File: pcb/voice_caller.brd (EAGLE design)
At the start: 56.5 x 59.1 mm, 36 parts, among them IC1 PRO_MICRO, IC2 AT45DB321D-S, IC3 78L12SMD, K1 TQ2SA-L2-5V

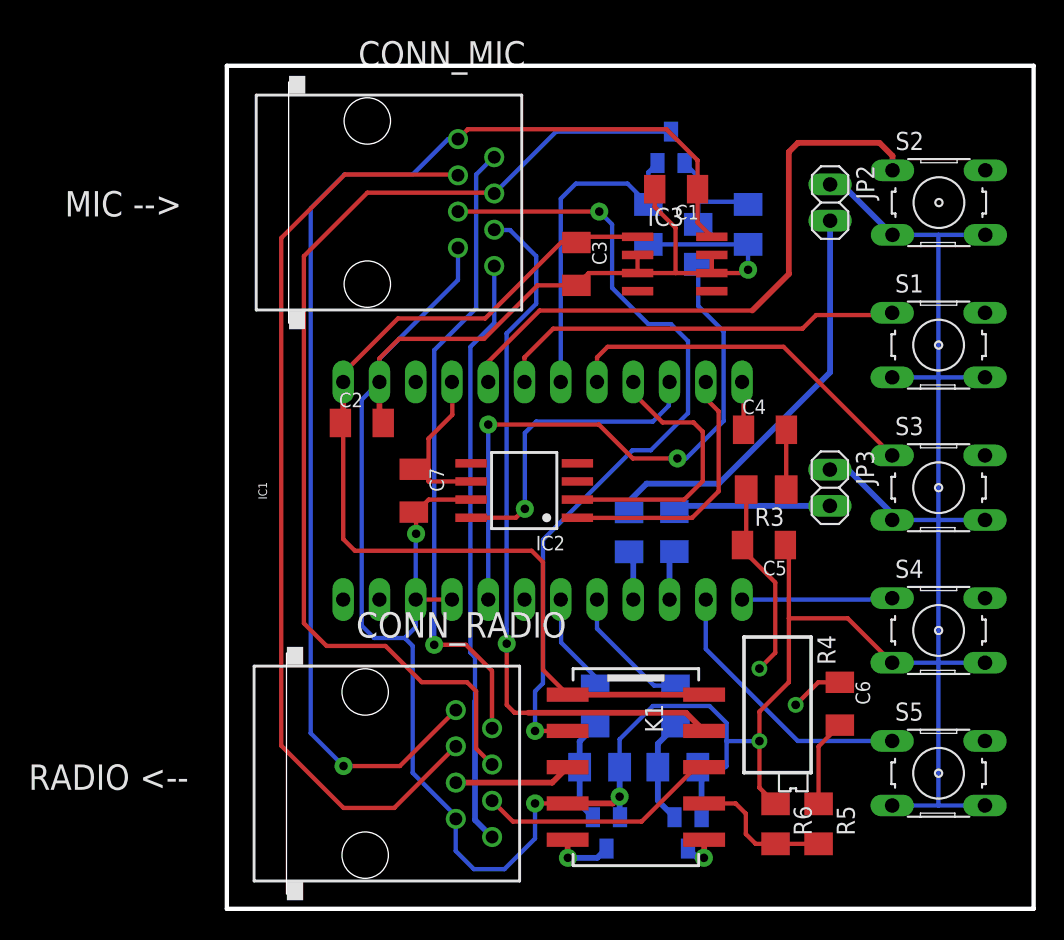
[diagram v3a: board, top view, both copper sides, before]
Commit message: Mounting holes
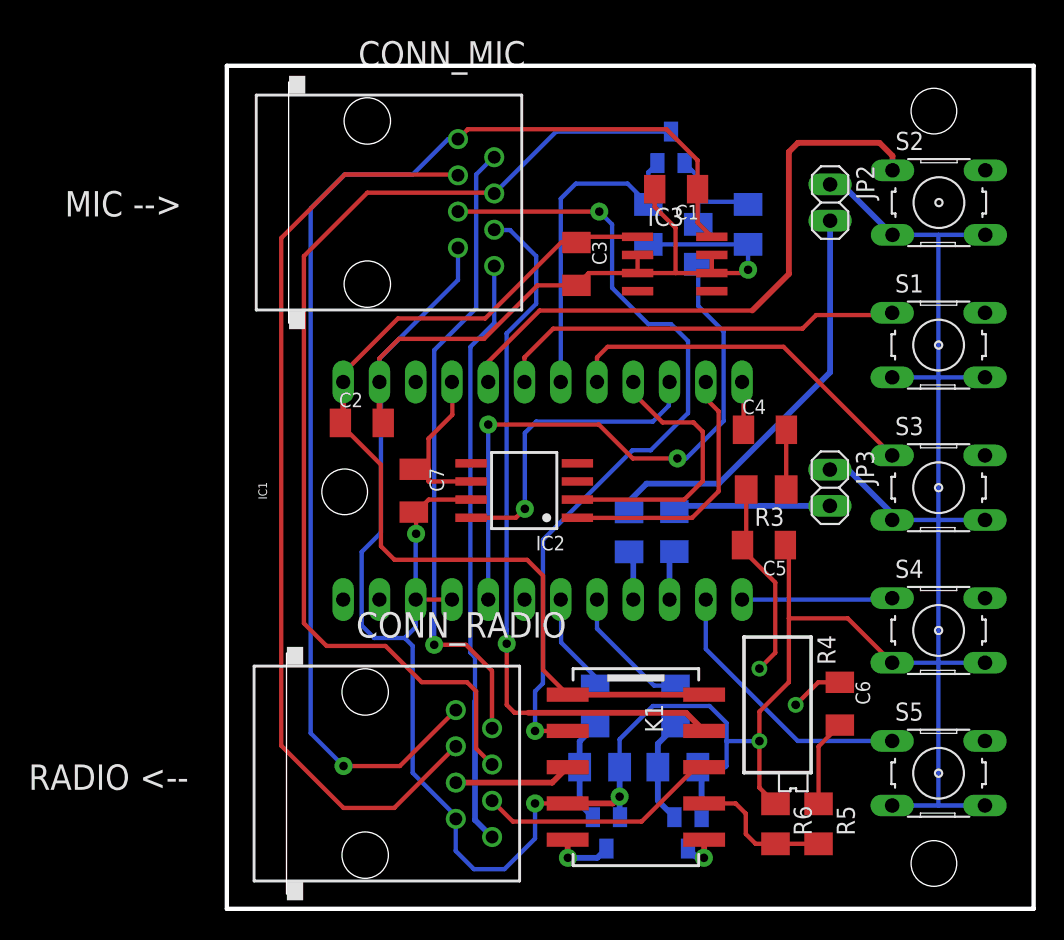
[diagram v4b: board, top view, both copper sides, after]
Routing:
- net +5V: track 70.8 -> 69.1 mm
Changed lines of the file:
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@@
 <layer number="42" name="bRestrict" color="1" fill="10" visible="yes" active="yes"/>
 <layer number="43" name="vRestrict" color="2" fill="10" visible="yes" active="yes"/>
-<layer number="44" name="Drills" color="7" fill="1" visible="no" active="yes"/>
-<layer number="45" name="Holes" color="7" fill="1" visible="no" active="yes"/>
+<layer number="44" name="Drills" color="7" fill="1" visible="yes" active="yes"/>
+<layer number="45" name="Holes" color="7" fill="1" visible="yes" active="yes"/>
 <layer number="46" name="Milling" color="3" fill="1" visible="no" active="yes"/>
 <layer number="47" name="Measures" color="7" fill="1" visible="no" active="yes"/>
@@
 <wire x1="62.865" y1="5.715" x2="62.865" y2="64.77" width="0.3048" layer="20"/>
 <wire x1="62.865" y1="64.77" x2="6.35" y2="64.77" width="0.3048" layer="20"/>
+<hole x="55.88" y="8.89" drill="3.2"/>
+<hole x="55.88" y="61.595" drill="3.2"/>
+<hole x="14.605" y="34.925" drill="3.2"/>
 </plain>
 <attributes>
@@
 <contactref element="K1" pad="10"/>
 <wire x1="39.784375" y1="20.716875" x2="30.224375" y2="20.716875" width="0.4064" layer="1"/>
-<wire x1="14.5" y1="39.752528125" x2="14.5" y2="31.616875" width="0.3048" layer="1"/>
-<wire x1="14.5" y1="31.616875" x2="15.319375" y2="30.7975" width="0.3048" layer="1"/>
-<wire x1="15.319375" y1="30.7975" x2="27.701875" y2="30.7975" width="0.3048" layer="1"/>
-<wire x1="27.701875" y1="30.7975" x2="28.495625" y2="30.00375" width="0.3048" layer="1"/>
-<wire x1="28.495625" y1="30.00375" x2="28.495625" y2="22.445625" width="0.3048" layer="1"/>
+<wire x1="27.384375" y1="30.1625" x2="28.495625" y2="29.05125" width="0.3048" layer="1"/>
+<wire x1="28.495625" y1="29.05125" x2="28.495625" y2="22.445625" width="0.3048" layer="1"/>
 <wire x1="28.495625" y1="22.445625" x2="30.224375" y2="20.716875" width="0.3048" layer="1"/>
 <wire x1="29.766875" y1="52.38875" x2="30.8375" y2="52.38875" width="0.3048" layer="1"/>
+<wire x1="27.384375" y1="30.1625" x2="18.0975" y2="30.1625" width="0.3048" layer="1"/>
+<wire x1="18.0975" y1="30.1625" x2="17.145" y2="31.115" width="0.3048" layer="1"/>
+<wire x1="17.145" y1="31.115" x2="17.145" y2="36.83" width="0.3048" layer="1"/>
+<wire x1="17.145" y1="36.83" x2="14.303696875" y2="39.671303125" width="0.3048" layer="1"/>
+<wire x1="14.303696875" y1="39.671303125" x2="14.303696875" y2="39.752528125" width="0.3048" layer="1"/>
 </signal>
 <signal name="GND">
@@
 <wire x1="18.811875" y1="24.685625" x2="16.66875" y2="24.685625" width="0.3048" layer="16"/>
 <wire x1="16.66875" y1="24.685625" x2="15.795625" y2="25.55875" width="0.3048" layer="16"/>
-<wire x1="15.795625" y1="25.55875" x2="15.795625" y2="41.375625" width="0.3048" layer="16"/>
-<wire x1="15.795625" y1="41.375625" x2="17.04" y2="42.62" width="0.3048" layer="16"/>
 <wire x1="17.04" y1="42.62" x2="17.04" y2="44.265625" width="0.3048" layer="16"/>
 <wire x1="17.04" y1="44.265625" x2="22.5425" y2="49.768125" width="0.3048" layer="16"/>
@@
 <wire x1="48.6085875" y1="56.458184375" x2="49.448140625" y2="56.458184375" width="0.4064" layer="16"/>
 <wire x1="49.448140625" y1="56.458184375" x2="52.9813" y2="52.925025" width="0.4064" layer="16"/>
+<wire x1="17.04" y1="42.62" x2="17.145" y2="42.515" width="0.3048" layer="16"/>
+<wire x1="17.145" y1="42.515" x2="17.145" y2="32.0675" width="0.3048" layer="16"/>
+<wire x1="17.145" y1="32.0675" x2="15.795625" y2="30.718125" width="0.3048" layer="16"/>
+<wire x1="15.795625" y1="30.718125" x2="15.795625" y2="25.55875" width="0.3048" layer="16"/>
 </signal>
 <signal name="MOSI">

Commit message: Missing nets for flash routed.
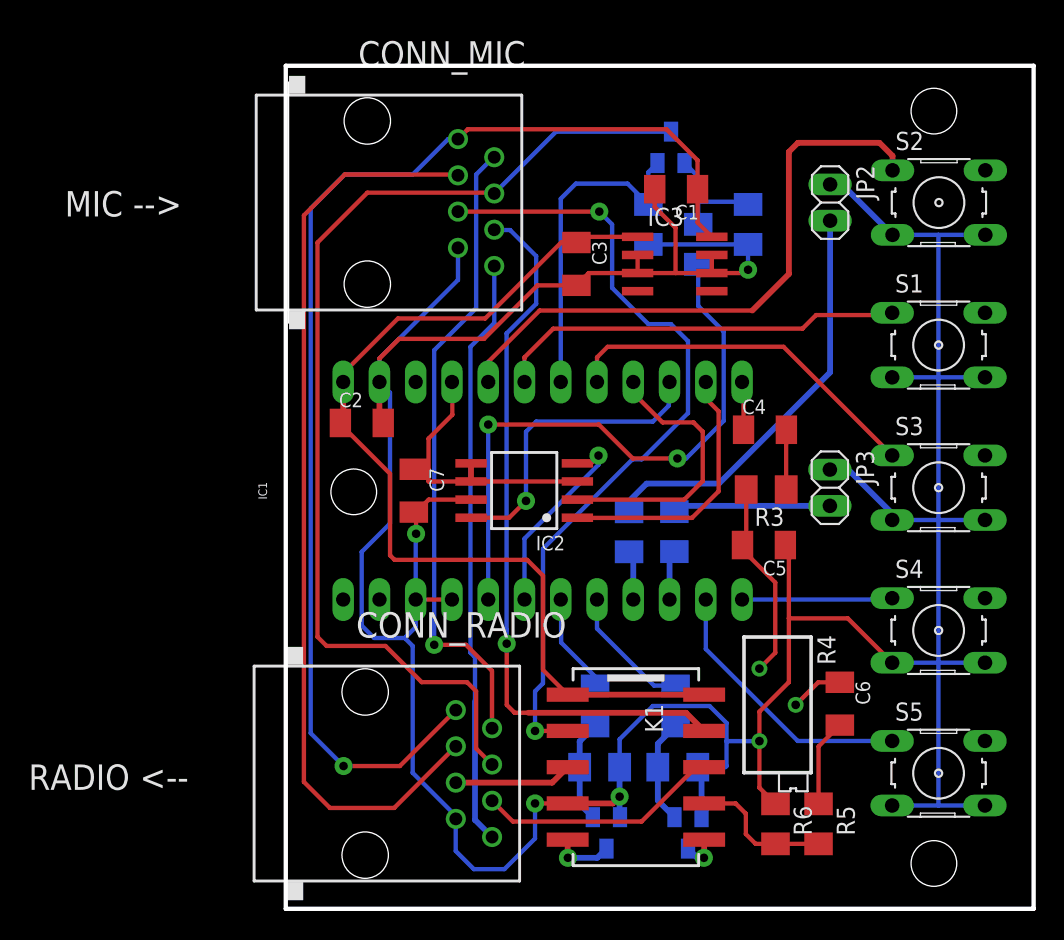
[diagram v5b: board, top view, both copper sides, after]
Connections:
- removed net N$7: IC2.5
- removed net N$8: IC2.3
- net +3V3: now also IC2.3, IC2.5
- net FLASH_CS: now also IC1.6
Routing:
- net FLASH_CS: track 0.00 -> 14.2 mm, vias 0 -> 1
- net +3V3: track 11.7 -> 20.4 mm
- net PTT: track 74.7 -> 73.9 mm
- net AF_OUT: track 65.6 -> 64.9 mm
- net GND: track 270.6 -> 271.2 mm
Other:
- board size 56.5 x 59.1 mm -> 52.4 x 59.1 mm
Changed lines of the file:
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@@
 <layer number="42" name="bRestrict" color="1" fill="10" visible="yes" active="yes"/>
 <layer number="43" name="vRestrict" color="2" fill="10" visible="yes" active="yes"/>
-<layer number="44" name="Drills" color="7" fill="1" visible="yes" active="yes"/>
-<layer number="45" name="Holes" color="7" fill="1" visible="yes" active="yes"/>
+<layer number="44" name="Drills" color="7" fill="1" visible="no" active="yes"/>
+<layer number="45" name="Holes" color="7" fill="1" visible="no" active="yes"/>
 <layer number="46" name="Milling" color="3" fill="1" visible="no" active="yes"/>
 <layer number="47" name="Measures" color="7" fill="1" visible="no" active="yes"/>
@@
 <text x="-5.000625" y="54.213125" size="1.778" layer="21">MIC --&gt;</text>
 <text x="-7.540625" y="14.049375" size="1.778" layer="21">RADIO &lt;--</text>
-<wire x1="6.35" y1="64.77" x2="6.35" y2="5.715" width="0.3048" layer="20"/>
-<wire x1="6.35" y1="5.715" x2="62.865" y2="5.715" width="0.3048" layer="20"/>
+<wire x1="10.4775" y1="64.77" x2="10.4775" y2="5.715" width="0.3048" layer="20"/>
+<wire x1="10.4775" y1="5.715" x2="62.865" y2="5.715" width="0.3048" layer="20"/>
 <wire x1="62.865" y1="5.715" x2="62.865" y2="64.77" width="0.3048" layer="20"/>
-<wire x1="62.865" y1="64.77" x2="6.35" y2="64.77" width="0.3048" layer="20"/>
+<wire x1="62.865" y1="64.77" x2="10.4775" y2="64.77" width="0.3048" layer="20"/>
 <hole x="55.88" y="8.89" drill="3.2"/>
 <hole x="55.88" y="61.595" drill="3.2"/>
-<hole x="14.605" y="34.925" drill="3.2"/>
+<hole x="15.24" y="34.925" drill="3.2"/>
 </plain>
 <attributes>
@@
 </class>
 </classes>
-<designrules name="default">
+<designrules name="default *">
 <description language="de">&lt;b&gt;EAGLE Design Rules&lt;/b&gt;
 &lt;p&gt;
@@
 <param name="mdPadVia" value="8mil"/>
 <param name="mdViaVia" value="8mil"/>
-<param name="mdSmdPad" value="8mil"/>
-<param name="mdSmdVia" value="8mil"/>
-<param name="mdSmdSmd" value="8mil"/>
+<param name="mdSmdPad" value="0mil"/>
+<param name="mdSmdVia" value="0mil"/>
+<param name="mdSmdSmd" value="0mil"/>
 <param name="mdViaViaSameLayer" value="8mil"/>
 <param name="mnLayersViaInSmd" value="2"/>
@@
 <wire x1="29.766875" y1="52.38875" x2="30.8375" y2="52.38875" width="0.3048" layer="1"/>
 <wire x1="27.384375" y1="30.1625" x2="18.0975" y2="30.1625" width="0.3048" layer="1"/>
-<wire x1="18.0975" y1="30.1625" x2="17.145" y2="31.115" width="0.3048" layer="1"/>
-<wire x1="17.145" y1="31.115" x2="17.145" y2="36.83" width="0.3048" layer="1"/>
-<wire x1="17.145" y1="36.83" x2="14.303696875" y2="39.671303125" width="0.3048" layer="1"/>
+<wire x1="18.0975" y1="30.1625" x2="17.78" y2="30.48" width="0.3048" layer="1"/>
+<wire x1="17.78" y1="30.48" x2="17.78" y2="36.195" width="0.3048" layer="1"/>
+<wire x1="17.78" y1="36.195" x2="14.303696875" y2="39.671303125" width="0.3048" layer="1"/>
 <wire x1="14.303696875" y1="39.671303125" x2="14.303696875" y2="39.752528125" width="0.3048" layer="1"/>
 </signal>
@@
 <wire x1="48.6085875" y1="56.458184375" x2="49.448140625" y2="56.458184375" width="0.4064" layer="16"/>
 <wire x1="49.448140625" y1="56.458184375" x2="52.9813" y2="52.925025" width="0.4064" layer="16"/>
-<wire x1="17.04" y1="42.62" x2="17.145" y2="42.515" width="0.3048" layer="16"/>
-<wire x1="17.145" y1="42.515" x2="17.145" y2="32.0675" width="0.3048" layer="16"/>
-<wire x1="17.145" y1="32.0675" x2="15.795625" y2="30.718125" width="0.3048" layer="16"/>
+<wire x1="17.04" y1="42.62" x2="17.78" y2="41.88" width="0.3048" layer="16"/>
+<wire x1="17.78" y1="41.88" x2="17.78" y2="32.7025" width="0.3048" layer="16"/>
+<wire x1="17.78" y1="32.7025" x2="15.795625" y2="30.718125" width="0.3048" layer="16"/>
 <wire x1="15.795625" y1="30.718125" x2="15.795625" y2="25.55875" width="0.3048" layer="16"/>
 </signal>
@@
 <contactref element="IC2" pad="8"/>
 <contactref element="IC1" pad="15"/>
-<wire x1="23.455" y1="33.11" x2="26.60125" y2="33.11" width="0.3048" layer="1"/>
-<wire x1="26.60125" y1="33.11" x2="27.225625" y2="33.734375" width="0.3048" layer="1"/>
-<wire x1="27.225625" y1="33.734375" x2="27.225625" y2="39.0525" width="0.3048" layer="16"/>
-<wire x1="27.225625" y1="39.0525" x2="28.019375" y2="39.84625" width="0.3048" layer="16"/>
 <wire x1="28.019375" y1="39.84625" x2="36.195" y2="39.84625" width="0.3048" layer="16"/>
 <wire x1="36.195" y1="39.84625" x2="37.30625" y2="40.9575" width="0.3048" layer="16"/>
 <wire x1="37.30625" y1="40.9575" x2="37.30625" y2="42.56625" width="0.3048" layer="16"/>
 <wire x1="37.30625" y1="42.56625" x2="37.36" y2="42.62" width="0.3048" layer="16"/>
-<via x="27.225625" y="33.734375" extent="1-16" drill="0.6" diameter="1.27" shape="square"/>
+<wire x1="23.455" y1="33.11" x2="26.125" y2="33.11" width="0.3048" layer="1"/>
+<wire x1="26.125" y1="33.11" x2="27.305" y2="34.29" width="0.3048" layer="1"/>
+<via x="27.305" y="34.29" extent="1-16" drill="0.6" diameter="1.27" shape="square"/>
+<wire x1="27.305" y1="34.29" x2="27.305" y2="39.131875" width="0.3048" layer="16"/>
+<wire x1="27.305" y1="39.131875" x2="28.019375" y2="39.84625" width="0.3048" layer="16"/>
 </signal>
 <signal name="SCK">
@@
 <signal name="FLASH_CS">
 <contactref element="IC2" pad="4"/>
-</signal>
-<signal name="N$7">
-<contactref element="IC2" pad="5"/>
-</signal>
-<signal name="N$8">
-<contactref element="IC2" pad="3"/>
+<contactref element="IC1" pad="6"/>
+<via x="32.385" y="37.465" extent="1-16" drill="0.6" diameter="1.27" shape="square"/>
+<wire x1="27.2" y1="27.38" x2="27.2" y2="31.645" width="0.3048" layer="16"/>
+<wire x1="27.2" y1="31.645" x2="32.385" y2="36.83" width="0.3048" layer="16"/>
+<wire x1="32.385" y1="36.83" x2="32.385" y2="37.465" width="0.3048" layer="16"/>
+<wire x1="30.905" y1="36.92" x2="30.7975" y2="37.0275" width="0.3048" layer="1"/>
+<wire x1="30.7975" y1="37.0275" x2="31.9475" y2="37.0275" width="0.3048" layer="1"/>
+<wire x1="31.9475" y1="37.0275" x2="32.385" y2="37.465" width="0.3048" layer="1"/>
 </signal>
 <signal name="PTT">
@@
 <wire x1="25.08" y1="55.825" x2="25.025" y2="55.88" width="0.3048" layer="1"/>
 <wire x1="25.025" y1="55.88" x2="16.1925" y2="55.88" width="0.3048" layer="1"/>
-<wire x1="16.1925" y1="55.88" x2="11.7475" y2="51.435" width="0.3048" layer="1"/>
-<wire x1="11.7475" y1="51.435" x2="11.7475" y2="25.7175" width="0.3048" layer="1"/>
-<wire x1="11.7475" y1="25.7175" x2="13.335" y2="24.13" width="0.3048" layer="1"/>
+<wire x1="12.7" y1="52.3875" x2="12.7" y2="24.765" width="0.3048" layer="1"/>
 <wire x1="13.335" y1="24.13" x2="17.4625" y2="24.13" width="0.3048" layer="1"/>
 <wire x1="17.4625" y1="24.13" x2="20.0025" y2="21.59" width="0.3048" layer="1"/>
@@
 <wire x1="37.465" y1="60.155" x2="29.41" y2="60.155" width="0.3048" layer="16"/>
 <wire x1="29.41" y1="60.155" x2="25.08" y2="55.825" width="0.3048" layer="16"/>
+<wire x1="12.7" y1="52.3875" x2="16.1925" y2="55.88" width="0.3048" layer="1"/>
+<wire x1="12.7" y1="24.765" x2="13.335" y2="24.13" width="0.3048" layer="1"/>
 </signal>
 <signal name="+8V">
@@
 <contactref element="CONN_MIC" pad="3"/>
 <contactref element="CONN_RADIO" pad="3"/>
-<wire x1="10.16" y1="52.705" x2="14.605" y2="57.15" width="0.3048" layer="1"/>
 <wire x1="14.605" y1="57.15" x2="22.485" y2="57.15" width="0.3048" layer="1"/>
 <wire x1="22.485" y1="57.15" x2="22.54" y2="57.095" width="0.3048" layer="1"/>
-<wire x1="10.16" y1="17.145" x2="14.525625" y2="12.779375" width="0.3048" layer="1"/>
-<wire x1="14.525625" y1="12.779375" x2="18.074375" y2="12.779375" width="0.3048" layer="1"/>
+<wire x1="13.573125" y1="12.779375" x2="18.074375" y2="12.779375" width="0.3048" layer="1"/>
 <wire x1="18.074375" y1="12.779375" x2="22.39" y2="17.095" width="0.3048" layer="1"/>
-<wire x1="10.16" y1="52.705" x2="10.16" y2="17.145" width="0.3048" layer="1"/>
+<wire x1="11.7475" y1="54.2925" x2="11.7475" y2="14.605" width="0.3048" layer="1"/>
+<wire x1="11.7475" y1="54.2925" x2="14.605" y2="57.15" width="0.3048" layer="1"/>
+<wire x1="11.7475" y1="14.605" x2="13.573125" y2="12.779375" width="0.3048" layer="1"/>
 </signal>
 <signal name="MIC">
@@
 <wire x1="27.94" y1="18.176875" x2="30.224375" y2="18.176875" width="0.3048" layer="1"/>
 <wire x1="27.94" y1="20.955" x2="27.94" y2="18.176875" width="0.3048" layer="16"/>
-<wire x1="28.495625" y1="31.570625" x2="28.495625" y2="21.510625" width="0.3048" layer="16"/>
+<wire x1="28.495625" y1="30.935625" x2="28.495625" y2="21.510625" width="0.3048" layer="16"/>
 <wire x1="28.495625" y1="21.510625" x2="27.94" y2="20.955" width="0.3048" layer="16"/>
 <via x="32.44" y="54.555" extent="1-16" drill="0.6" diameter="1.27"/>
@@
 <wire x1="37.465" y1="46.6725" x2="38.655625" y2="45.481875" width="0.3048" layer="16"/>
 <wire x1="38.655625" y1="45.481875" x2="38.655625" y2="40.443125" width="0.3048" layer="16"/>
-<wire x1="38.655625" y1="40.443125" x2="36.05" y2="37.8375" width="0.3048" layer="16"/>
-<wire x1="36.05" y1="37.8375" x2="34.7625" y2="37.8375" width="0.3048" layer="16"/>
-<wire x1="34.7625" y1="37.8375" x2="28.495625" y2="31.570625" width="0.3048" layer="16"/>
+<wire x1="38.655625" y1="40.443125" x2="35.415" y2="37.2025" width="0.3048" layer="16"/>
+<wire x1="35.415" y1="37.2025" x2="34.7625" y2="37.2025" width="0.3048" layer="16"/>
+<wire x1="34.7625" y1="37.2025" x2="28.495625" y2="30.935625" width="0.3048" layer="16"/>
 </signal>
 <signal name="MIC_PWM">
@@
 <wire x1="19.446875" y1="36.504375" x2="20.47875" y2="36.504375" width="0.3048" layer="1"/>
 <wire x1="20.47875" y1="35.65" x2="20.47875" y2="36.504375" width="0.3048" layer="1"/>
+<contactref element="IC2" pad="3"/>
+<contactref element="IC2" pad="5"/>
+<wire x1="23.455" y1="35.65" x2="23.455" y2="36.92" width="0.4064" layer="1"/>
+<wire x1="30.905" y1="35.65" x2="23.455" y2="35.65" width="0.3048" layer="1"/>
 </signal>
 <signal name="N$6">
